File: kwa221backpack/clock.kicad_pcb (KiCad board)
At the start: 2 copper layers, 48.3 x 78.7 mm, 10 parts, among them U1 TLC5940NT

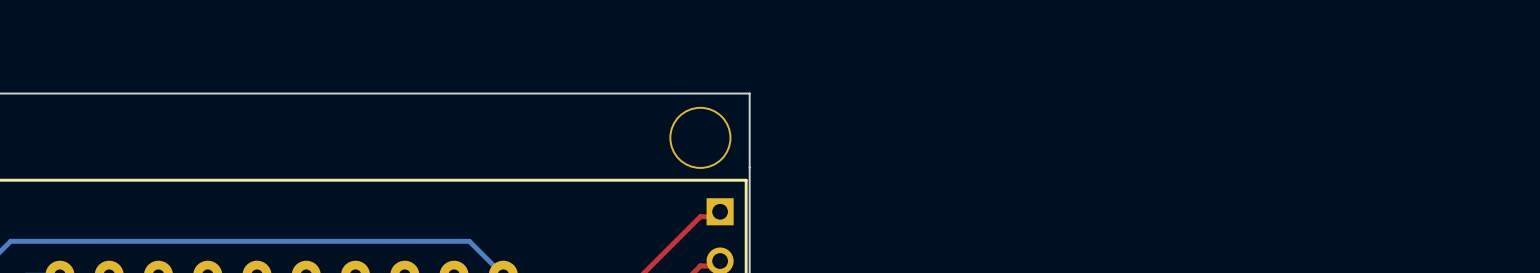
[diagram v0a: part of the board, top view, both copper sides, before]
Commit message: Moving outputs to a v1 directory so we can eventually generate a v2
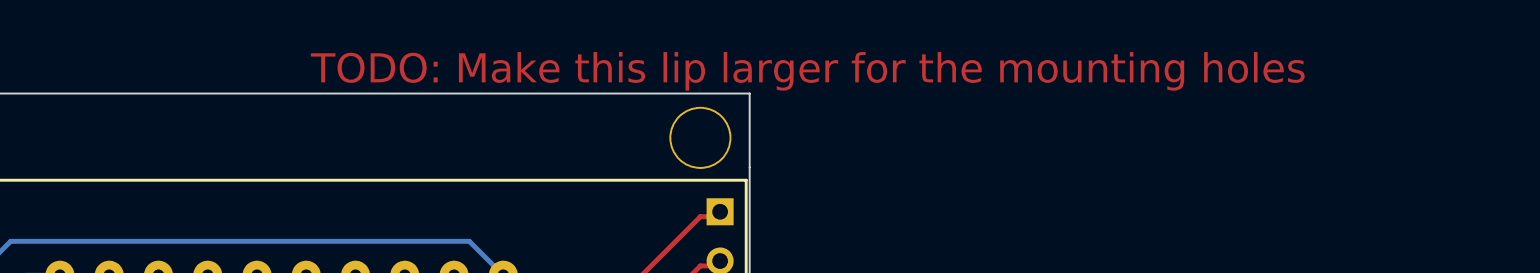
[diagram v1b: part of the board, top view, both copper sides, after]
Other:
- board text added: "TODO: Make this lip larger for the mounting holes"
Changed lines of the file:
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@@
     (area 39.352858 34.239999 101.357712 113.080001)
     (thickness 1.6)
-    (drawings 24)
+    (drawings 25)
     (tracks 206)
     (zones 0)
@@
     )
   )
+  (gr_text "TODO: Make this lip larger for the mounting holes" (at 99.568 33.02) (layer F.Cu)
+    (effects (font (size 1.5 1.5) (thickness 0.3)))
+  )
   (gr_line (start 96.52 34.29) (end 96.52 38.1) (angle 90) (layer Edge.Cuts) (width 0.1))
